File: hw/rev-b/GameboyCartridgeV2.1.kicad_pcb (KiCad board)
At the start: 6 copper layers, 52.8 x 61.2 mm, 148 parts, among them J1 USB_C_Receptacle_USB2.0, J2 Micro_SD_Card_Det2, J4 Conn_01x06, J5 CartBus, Q1 CJ2302, Q101 SIA975DJ-T1-GE3, Q102 2N7002, SW1 SW_Push, SW2 SW_Push, U1 USBLC6-2P6, U101 TPS2116DRLR, U102 TPS2553DBVR, U103 TPS63802DLAR, U104 ESP32-C3-MINI-1U-N4, U105 SN74LVC1G125DBVR, U106 SN74LVC3G34DCTR, U107 CH334P, U108 TLV3012BIDBVR, U109 TLV431BIDBZR, U2 W25Q16JVSSIQ, U3 RP2350_80QFN, U4 W956A8MBYA5I, U5 MCP79510, U6 AP2112K-3.3, U7 TXB0108PW, Y1 12MHz, Y101 12MHz 10pF 10ppm, Y2 32.768kHz

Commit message: routing: GND via-in-pad (U5, C102 area), +3V3_RF/LIM_FAULT_N/GB_CS re-routed, VCC to U101 via In4 VCC plane extension + one via (router's 108 mm detour rejected), GB_A2 jogged; 5 open; tools pad_to_plane, dump_region, plot_layers
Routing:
- net /Radio/ESP_IO2_MISO: track 30.1 -> 25.3 mm
- net /Radio/+3V3_RF: track 89.5 -> 93.4 mm, vias 6 -> 7
- net /Radio/LIM_FAULT_N: track 29.9 -> 33.4 mm, vias 3 -> 5
- net GB_CS: track 35.6 -> 38.0 mm, vias 1 -> 2
- net VCC: vias 5 -> 6
- net GND: vias 212 -> 214

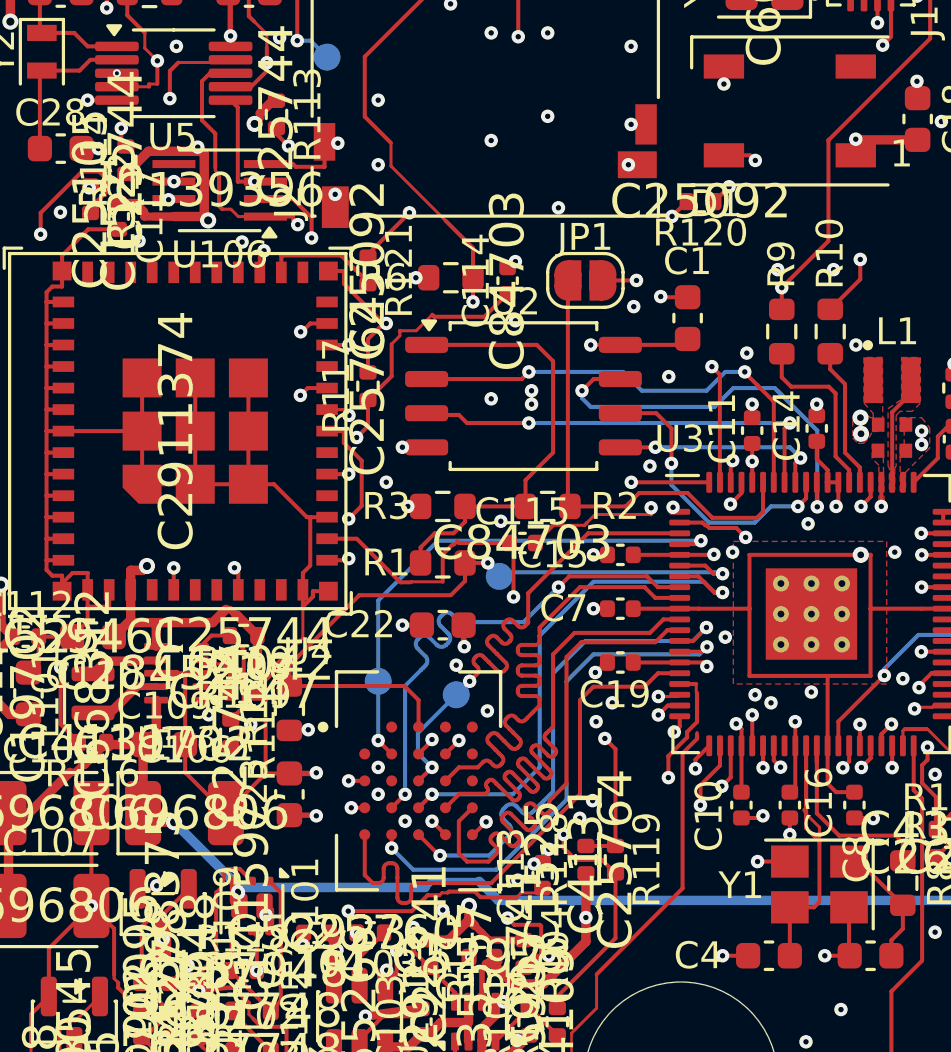
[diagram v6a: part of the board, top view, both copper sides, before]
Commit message: routing: ESP MISO/MOSI, GB_A7 escape (GB_A6 via moved, GB_A5 via 0.35/0.15), dead GB_A7 stub removed; 2 open; tools via_to_track, route_pair, FR_VIA
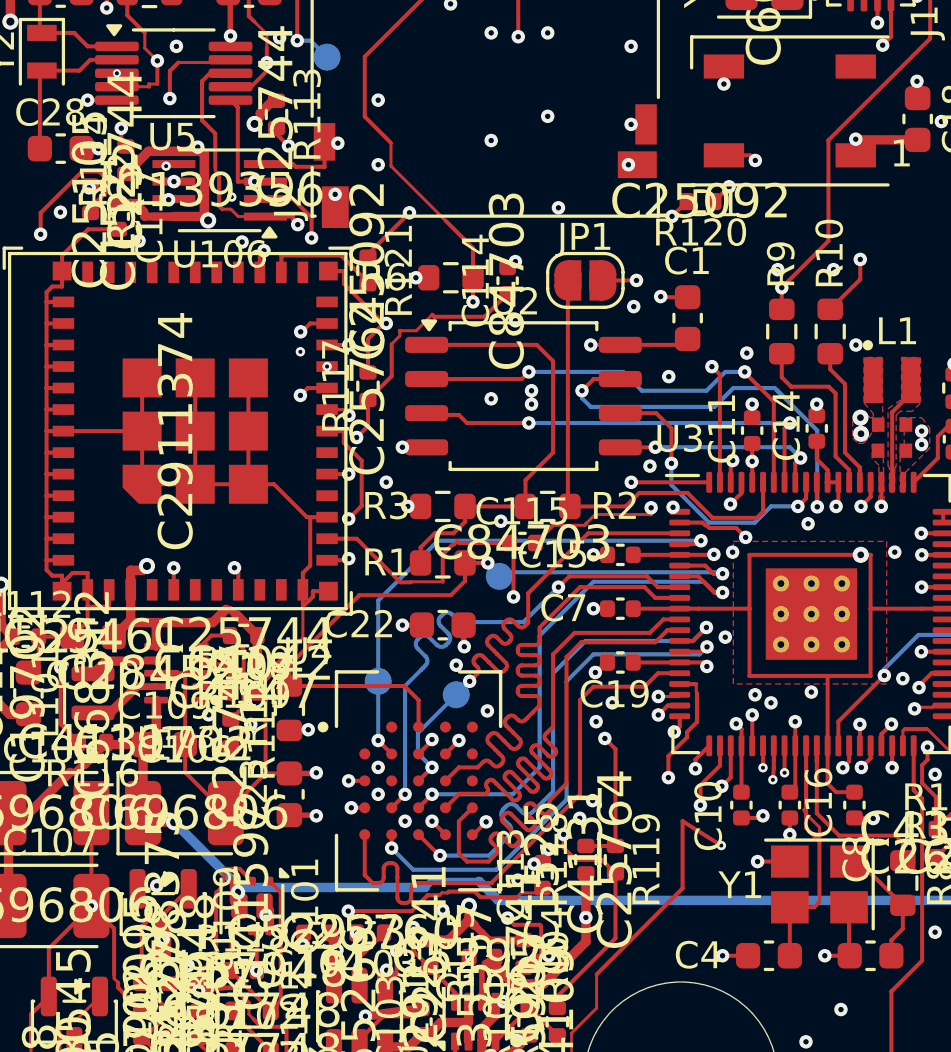
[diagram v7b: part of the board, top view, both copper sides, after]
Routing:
- net /Radio/ESP_MOSI: track 0.00 -> 11.2 mm, vias 0 -> 4
- net /Radio/ESP_IO2_MISO: track 25.3 -> 30.2 mm
- net GB_A7: track 23.4 -> 26.4 mm, vias 0 -> 2

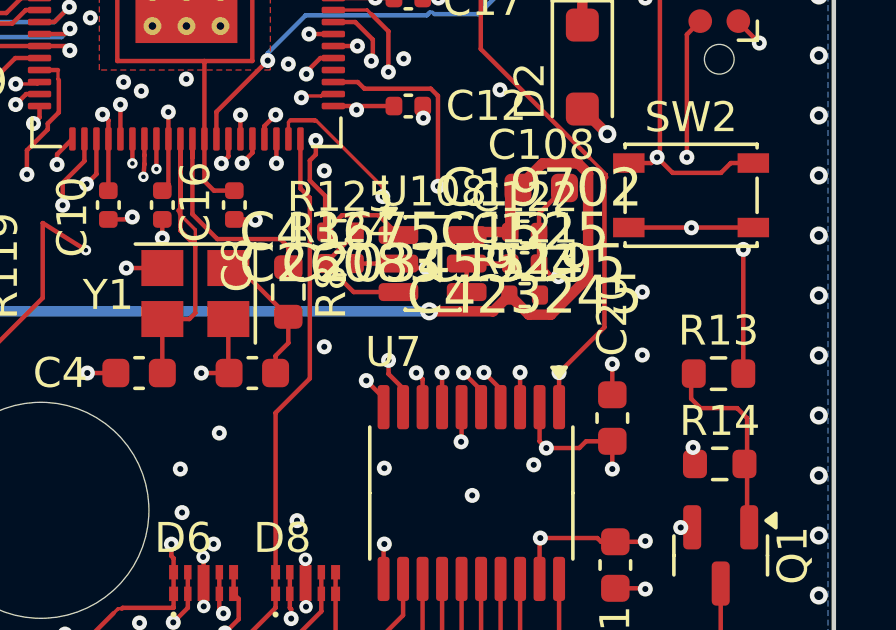
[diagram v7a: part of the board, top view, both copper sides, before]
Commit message: R123 (1.3M PG_SENSE top resistor) moved next to U108 pin 3, VRES end drops onto the B.Cu VRES run; PG_SENSE connected; 1 open (GB_A15)
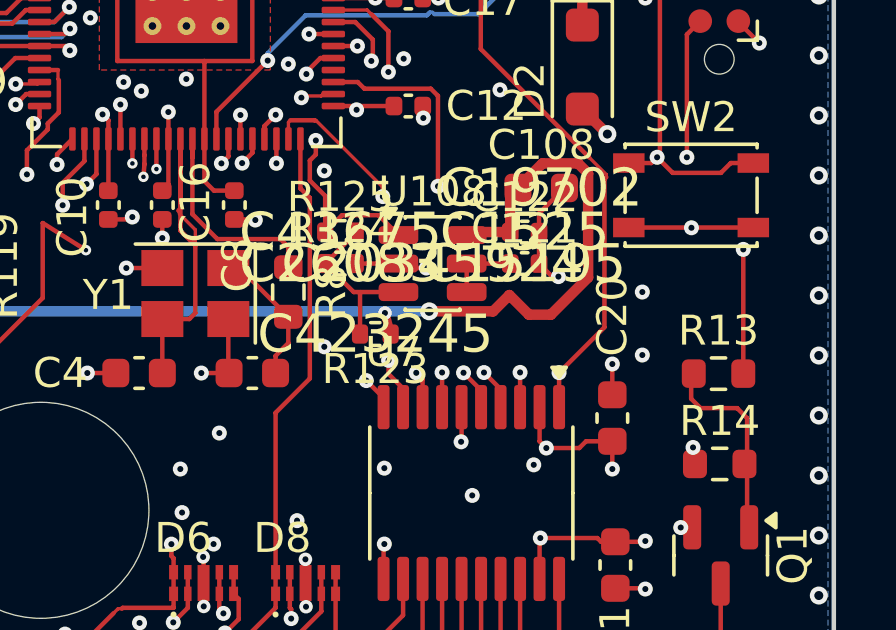
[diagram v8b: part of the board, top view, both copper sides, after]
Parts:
- moved R123 5.14 mm to (150.9, 102.2), turned to 180 degrees
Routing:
- net /Radio/PG_SENSE: track 4.31 -> 5.71 mm
- net VRES: track 65.8 -> 66.5 mm, vias 4 -> 5
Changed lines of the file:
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@@
 	(footprint "Resistor_SMD:R_0402_1005Metric"
 		(layer "F.Cu")
-		(at 155.878 100.901)
+		(at 150.9 102.2 180)
 		(descr "Resistor SMD 0402 (1005 Metric), square (rectangular) end terminal, IPC-7351 nominal, (Body size source: IPC-SM-782 page 72, https://www.pcb-3d.com/wordpress/wp-content/uploads/ipc-sm-782a_amendment_1_and_2.pdf)")
 		(tags "resistor")
 		(property "Reference" "R123"
-			(at 0 -1.17 0)
+			(at 0 -1.17 180)
 			(layer "F.SilkS")
 			(effects
@@
 		)
 		(property "Value" "1.3M 1%"
-			(at 0 1.17 0)
+			(at 0 1.17 180)
 			(layer "F.Fab")
 			(effects
@@
 		)
 		(property "Datasheet" ""
-			(at 0 0 0)
+			(at 0 0 180)
 			(layer "F.Fab")
 			(hide yes)
@@
 		)
 		(property "Description" ""
-			(at 0 0 0)
+			(at 0 0 180)
 			(layer "F.Fab")
 			(hide yes)
@@
 		)
 		(property "KiLib_Generator" "SMD_2terminal_chip_molded"
-			(at 0 0 0)
+			(at 0 0 180)
 			(layer "F.SilkS")
 			(hide yes)
@@
 		)
 		(property "LCSC" "C423245"
-			(at 0 0 0)
+			(at 0 0 180)
 			(layer "F.SilkS")
 			(effects
@@
 		(duplicate_pad_numbers_are_jumpers no)
 		(fp_line
-			(start -0.153641 -0.38)
-			(end 0.153641 -0.38)
+			(start -0.153641 0.38)
+			(end 0.153641 0.38)
 			(stroke
 				(width 0.12)
@@
 		)
 		(fp_line
-			(start -0.153641 0.38)
-			(end 0.153641 0.38)
+			(start -0.153641 -0.38)
+			(end 0.153641 -0.38)
 			(stroke
 				(width 0.12)
@@
 		)
 		(fp_text user "${REFERENCE}"
-			(at 0 0 0)
+			(at 0 0 180)
 			(layer "F.Fab")
 			(effects
@@
 		)
 		(pad "1" smd roundrect
-			(at -0.51 0)
+			(at -0.51 0 180)
 			(size 0.54 0.64)
 			(layers "F.Cu" "F.Mask" "F.Paste")
@@
 		)
 		(pad "2" smd roundrect
-			(at 0.51 0)
+			(at 0.51 0 180)
 			(size 0.54 0.64)
 			(layers "F.Cu" "F.Mask" "F.Paste")
@@
 	)
 	(segment
+		(start 151.41 102.2)
+		(end 151.22 101.5)
+		(width 0.3)
+		(layer "F.Cu")
+		(net "VRES")
+	)
+	(segment
 		(start 157.9932 96.8465)
 		(end 157.9932 100.3141)
@@
 		(net "VRES")
 	)
+	(via
+		(at 151.22 101.5)
+		(size 0.45)
+		(drill 0.2)
+		(layers "F.Cu" "B.Cu")
+		(net "VRES")
+	)
 	(segment
 		(start 152.6966 101.4438)
@@
 		(width 0.15)
 		(layer "F.Cu")
+		(net "/Radio/PG_SENSE")
+	)
+	(segment
+		(start 150.39 102.2)
+		(end 150.39 100.801)
+		(width 0.15)
+		(layer "F.Cu")
